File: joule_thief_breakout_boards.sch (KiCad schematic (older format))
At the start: 13 parts

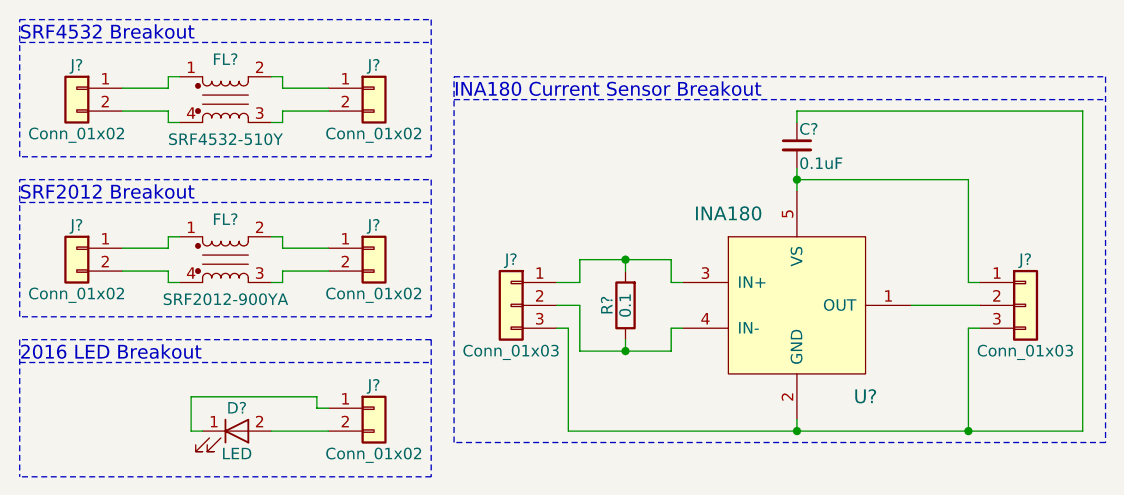
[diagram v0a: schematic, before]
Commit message: header pin swaping for easy lineup with pcb
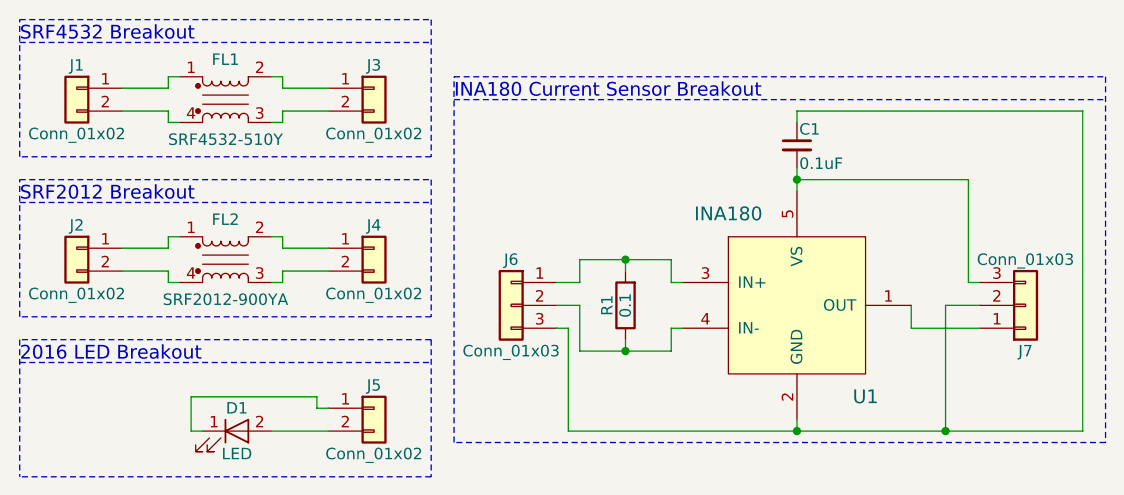
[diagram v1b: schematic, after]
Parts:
- C1: renamed from C?; footprint (none) -> Capacitors_SMD:C_0805_HandSoldering
- J1, J2, J3, J4, J5: renamed from J?; footprint (none) -> lib_fp:Etch_Pin_Header_Straight_1x02_Pitch2.54mm
- J6, J7: renamed from J?; footprint (none) -> lib_fp:Etch_Pin_Header_Straight_1x03_Pitch2.54mm
- R1: renamed from R?; footprint (none) -> Resistors_SMD:R_0805_HandSoldering
- U1: renamed from U?; footprint (none) -> TO_SOT_Packages_SMD:SOT-23-5_HandSoldering
- gave numbers to parts that had none: 3
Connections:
- net at U1.1 (OUT): now also J7.1 (Pin_1); no longer J7.2 (Pin_2)
- net at C1.1, J6.3 (Pin_3), U1.2 (GND): now also J7.2 (Pin_2); no longer J7.3 (Pin_3)
- net at C1.2, U1.5 (VS): now also J7.3 (Pin_3); no longer J7.1 (Pin_1)
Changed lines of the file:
@@
 LIBS:Bourns_EMI_Filter
 LIBS:Texas_Instruments
+LIBS:joule_thief_breakout_boards
 LIBS:power
 LIBS:device
@@
 $EndDescr
 $Comp
-L Bourns_Common_Mode_Inductor FL?
+L Bourns_Common_Mode_Inductor FL1
 U 1 1 59D17B36
 P 4200 3550
-F 0 "FL?" H 4200 3725 50  0000 C CNN
+F 0 "FL1" H 4200 3725 50  0000 C CNN
 F 1 "SRF4532-510Y" H 4200 3375 50  0000 C CNN
 F 2 "lib_fp:SRF4532_Bourns_CMI" V 4200 3590 50  0001 C CNN
@@
 $EndComp
 $Comp
-L Conn_01x02 J?
+L Conn_01x02 J3
 U 1 1 59D17D93
 P 4850 3500
-F 0 "J?" H 4850 3600 50  0000 C CNN
+F 0 "J3" H 4850 3600 50  0000 C CNN
 F 1 "Conn_01x02" H 4850 3300 50  0000 C CNN
-F 2 "" H 4850 3500 50  0001 C CNN
+F 2 "lib_fp:Etch_Pin_Header_Straight_1x02_Pitch2.54mm" H 4850 3500 50  0001 C CNN
 F 3 "" H 4850 3500 50  0001 C CNN
 	1    4850 3500
@@
 $EndComp
 $Comp
-L Conn_01x02 J?
+L Conn_01x02 J1
 U 1 1 59D17DBE
 P 3550 3500
-F 0 "J?" H 3550 3600 50  0000 C CNN
+F 0 "J1" H 3550 3600 50  0000 C CNN
 F 1 "Conn_01x02" H 3550 3300 50  0000 C CNN
-F 2 "" H 3550 3500 50  0001 C CNN
+F 2 "lib_fp:Etch_Pin_Header_Straight_1x02_Pitch2.54mm" H 3550 3500 50  0001 C CNN
 F 3 "" H 3550 3500 50  0001 C CNN
 	1    3550 3500
@@
 $EndComp
 $Comp
-L Bourns_Common_Mode_Inductor FL?
+L Bourns_Common_Mode_Inductor FL2
 U 1 1 59D17E74
 P 4200 4250
-F 0 "FL?" H 4200 4425 50  0000 C CNN
+F 0 "FL2" H 4200 4425 50  0000 C CNN
 F 1 "SRF2012-900YA" H 4200 4075 50  0000 C CNN
 F 2 "lib_fp:SRF2012_Bourns_CMI" V 4200 4290 50  0001 C CNN
@@
 $EndComp
 $Comp
-L Conn_01x02 J?
+L Conn_01x02 J4
 U 1 1 59D17E7A
 P 4850 4200
-F 0 "J?" H 4850 4300 50  0000 C CNN
+F 0 "J4" H 4850 4300 50  0000 C CNN
 F 1 "Conn_01x02" H 4850 4000 50  0000 C CNN
-F 2 "" H 4850 4200 50  0001 C CNN
+F 2 "lib_fp:Etch_Pin_Header_Straight_1x02_Pitch2.54mm" H 4850 4200 50  0001 C CNN
 F 3 "" H 4850 4200 50  0001 C CNN
 	1    4850 4200
@@
 $EndComp
 $Comp
-L Conn_01x02 J?
+L Conn_01x02 J2
 U 1 1 59D17E80
 P 3550 4200
-F 0 "J?" H 3550 4300 50  0000 C CNN
+F 0 "J2" H 3550 4300 50  0000 C CNN
 F 1 "Conn_01x02" H 3550 4000 50  0000 C CNN
-F 2 "" H 3550 4200 50  0001 C CNN
+F 2 "lib_fp:Etch_Pin_Header_Straight_1x02_Pitch2.54mm" H 3550 4200 50  0001 C CNN
 F 3 "" H 3550 4200 50  0001 C CNN
 	1    3550 4200
@@
 SRF2012 Breakout
 $Comp
-L LED D?
+L LED D1
 U 1 1 59D18B6B
 P 4250 5000
-F 0 "D?" H 4250 5100 50  0000 C CNN
+F 0 "D1" H 4250 5100 50  0000 C CNN
 F 1 "LED" H 4250 4900 50  0000 C CNN
 F 2 "lib_fp:LED_Luminus_MP-2016" H 4250 5000 50  0001 C CNN
@@
 $EndComp
 $Comp
-L Conn_01x02 J?
+L Conn_01x02 J5
 U 1 1 59D18CBF
 P 4850 4900
-F 0 "J?" H 4850 5000 50  0000 C CNN
+F 0 "J5" H 4850 5000 50  0000 C CNN
 F 1 "Conn_01x02" H 4850 4700 50  0000 C CNN
-F 2 "" H 4850 4900 50  0001 C CNN
+F 2 "lib_fp:Etch_Pin_Header_Straight_1x02_Pitch2.54mm" H 4850 4900 50  0001 C CNN
 F 3 "" H 4850 4900 50  0001 C CNN
 	1    4850 4900
@@
 2016 LED Breakout
 $Comp
-L INA180 U?
+L INA180 U1
 U 1 1 59D19901
 P 6700 4450
-F 0 "U?" H 7000 4050 60  0000 C CNN
+F 0 "U1" H 7000 4050 60  0000 C CNN
 F 1 "INA180" H 6400 4850 60  0000 C CNN
-F 2 "" H 6700 4450 60  0001 C CNN
+F 2 "TO_SOT_Packages_SMD:SOT-23-5_HandSoldering" H 6700 4450 60  0001 C CNN
 F 3 "" H 6700 4450 60  0001 C CNN
 	1    6700 4450
@@
 $EndComp
 $Comp
-L R R?
+L R R1
 U 1 1 59D19976
 P 5950 4450
-F 0 "R?" V 6030 4450 50  0000 C CNN
+F 0 "R1" V 6030 4450 50  0000 C CNN
 F 1 "0.1" V 5950 4450 50  0000 C CNN
-F 2 "" V 5880 4450 50  0001 C CNN
+F 2 "Resistors_SMD:R_0805_HandSoldering" V 5880 4450 50  0001 C CNN
 F 3 "" H 5950 4450 50  0001 C CNN
 F 4 "NONE" H 5950 4450 60  0001 C CNN "Manufacture"
@@
 $EndComp
 $Comp
-L Conn_01x03 J?
+L Conn_01x03 J7
 U 1 1 59D19C5E
 P 7700 4450
-F 0 "J?" H 7700 4650 50  0000 C CNN
+F 0 "J7" H 7700 4650 50  0000 C CNN
 F 1 "Conn_01x03" H 7700 4250 50  0000 C CNN
-F 2 "" H 7700 4450 50  0001 C CNN
+F 2 "lib_fp:Etch_Pin_Header_Straight_1x03_Pitch2.54mm" H 7700 4450 50  0001 C CNN
 F 3 "" H 7700 4450 50  0001 C CNN
 	1    7700 4450
-	1    0    0    -1
-$EndComp
-$Comp
-L Conn_01x03 J?
+	1    0    0    1
+$EndComp
+$Comp
+L Conn_01x03 J6
 U 1 1 59D19CC2
 P 5450 4450
-F 0 "J?" H 5450 4650 50  0000 C CNN
+F 0 "J6" H 5450 4650 50  0000 C CNN
 F 1 "Conn_01x03" H 5450 4250 50  0000 C CNN
-F 2 "" H 5450 4450 50  0001 C CNN
+F 2 "lib_fp:Etch_Pin_Header_Straight_1x03_Pitch2.54mm" H 5450 4450 50  0001 C CNN
 F 3 "" H 5450 4450 50  0001 C CNN
 	1    5450 4450
@@
 $EndComp
 $Comp
-L C_Small C?
+L C_Small C1
 U 1 1 59D1A6E2
 P 6700 3750
-F 0 "C?" H 6710 3820 50  0000 L CNN
+F 0 "C1" H 6710 3820 50  0000 L CNN
 F 1 "0.1uF" H 6710 3670 50  0000 L CNN
-F 2 "" H 6700 3750 50  0001 C CNN
+F 2 "Capacitors_SMD:C_0805_HandSoldering" H 6700 3750 50  0001 C CNN
 F 3 "" H 6700 3750 50  0001 C CNN
 F 4 "NONE" H 6700 3750 60  0001 C CNN "Manufacture"
@@
 Connection ~ 5950 4250
 Wire Wire Line
-	7200 4450 7500 4450
-Wire Wire Line
 	7500 4350 7450 4350
 Wire Wire Line
@@
 Wire Wire Line
 	6700 3850 6700 3950
-Wire Wire Line
-	7500 4550 7450 4550
-Wire Wire Line
-	7450 4550 7450 5000
 Wire Wire Line
 	5700 5000 7950 5000
@@
 Wire Wire Line
 	7950 3600 7950 5000
-Connection ~ 7450 5000
+Connection ~ 7350 5000
 Text Notes 5200 3550 0    60   ~ 0
 INA180 Current Sensor Breakout
@@
 Wire Notes Line
 	5200 3450 8050 3450
+Wire Wire Line
+	7350 5000 7350 4450
+Wire Wire Line
+	7350 4450 7500 4450
+Wire Wire Line
+	7200 4450 7200 4550
+Wire Wire Line
+	7200 4550 7500 4550
 $EndSCHEMATC

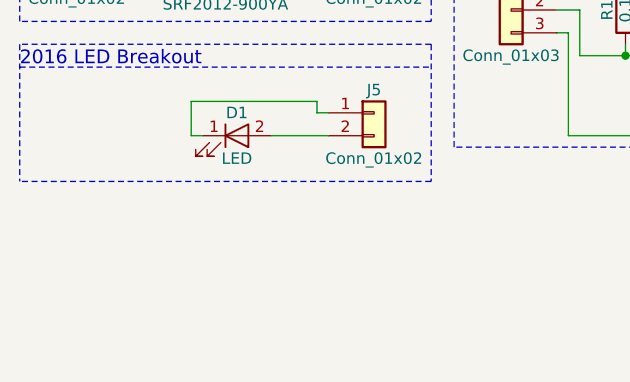
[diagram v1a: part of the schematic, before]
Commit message: add transistor breakout
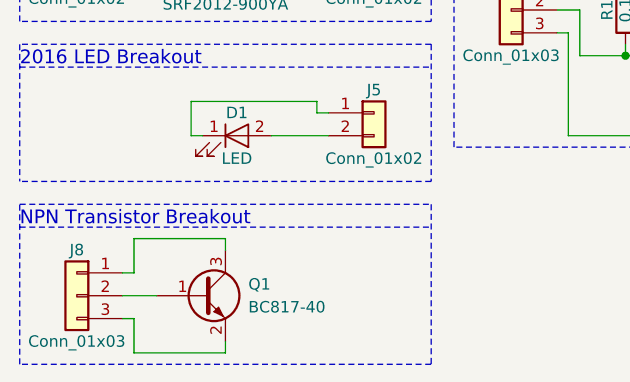
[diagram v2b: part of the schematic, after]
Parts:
- added J8: Conn_01x03, Pin_Headers:Pin_Header_Straight_1x03_Pitch2.54mm, symbol Conn_01x03
- added Q1: BC817-40, TO_SOT_Packages_SMD:SOT-23, symbol Q_NPN_BEC
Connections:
- new net: J8.2 (Pin_2), Q1.1 (B)
- new net: J8.3 (Pin_3), Q1.2 (E)
- new net: J8.1 (Pin_1), Q1.3 (C)
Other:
- note added: "NPN Transistor Breakout"
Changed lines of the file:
@@
 Wire Wire Line
 	7200 4550 7500 4550
+$Comp
+L Q_NPN_BEC Q1
+U 1 1 59D6C9FE
+P 4100 5700
+F 0 "Q1" H 4300 5750 50  0000 L CNN
+F 1 "BC817-40" H 4300 5650 50  0000 L CNN
+F 2 "TO_SOT_Packages_SMD:SOT-23" H 4300 5800 50  0001 C CNN
+F 3 "" H 4100 5700 50  0001 C CNN
+F 4 "NONE" H 4100 5700 60  0001 C CNN "Manufacture"
+F 5 "NONE" H 4100 5700 60  0001 C CNN "Mfg Part Number"
+F 6 "NONE" H 4100 5700 60  0001 C CNN "Package"
+F 7 "NONE" H 4100 5700 60  0001 C CNN "Description"
+	1    4100 5700
+	1    0    0    -1
+$EndComp
+$Comp
+L Conn_01x03 J8
+U 1 1 59D6CDE7
+P 3550 5700
+F 0 "J8" H 3550 5900 50  0000 C CNN
+F 1 "Conn_01x03" H 3550 5500 50  0000 C CNN
+F 2 "Pin_Headers:Pin_Header_Straight_1x03_Pitch2.54mm" H 3550 5700 50  0001 C CNN
+F 3 "" H 3550 5700 50  0001 C CNN
+	1    3550 5700
+	-1   0    0    -1
+$EndComp
+Wire Wire Line
+	3750 5700 3900 5700
+Wire Wire Line
+	3750 5600 3800 5600
+Wire Wire Line
+	3800 5600 3800 5450
+Wire Wire Line
+	3800 5450 4200 5450
+Wire Wire Line
+	4200 5450 4200 5500
+Wire Wire Line
+	3750 5800 3800 5800
+Wire Wire Line
+	3800 5800 3800 5950
+Wire Wire Line
+	3800 5950 4200 5950
+Wire Wire Line
+	4200 5950 4200 5900
+Text Notes 3300 5400 0    60   ~ 0
+NPN Transistor Breakout
+Wire Notes Line
+	3300 5400 5100 5400
+Wire Notes Line
+	5100 5300 5100 6000
+Wire Notes Line
+	5100 6000 3300 6000
+Wire Notes Line
+	3300 6000 3300 5300
+Wire Notes Line
+	3300 5300 5100 5300
 $EndSCHEMATC

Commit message: update CvPCB to reflect header footprint change in Pcbnew
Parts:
- J8: footprint Pin_Headers:Pin_Header_Straight_1x03_Pitch2.54mm -> lib_fp:Etch_Pin_Header_Straight_1x03_Pitch2.54mm
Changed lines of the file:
@@
 F 0 "J8" H 3550 5900 50  0000 C CNN
 F 1 "Conn_01x03" H 3550 5500 50  0000 C CNN
-F 2 "Pin_Headers:Pin_Header_Straight_1x03_Pitch2.54mm" H 3550 5700 50  0001 C CNN
+F 2 "lib_fp:Etch_Pin_Header_Straight_1x03_Pitch2.54mm" H 3550 5700 50  0001 C CNN
 F 3 "" H 3550 5700 50  0001 C CNN
 	1    3550 5700

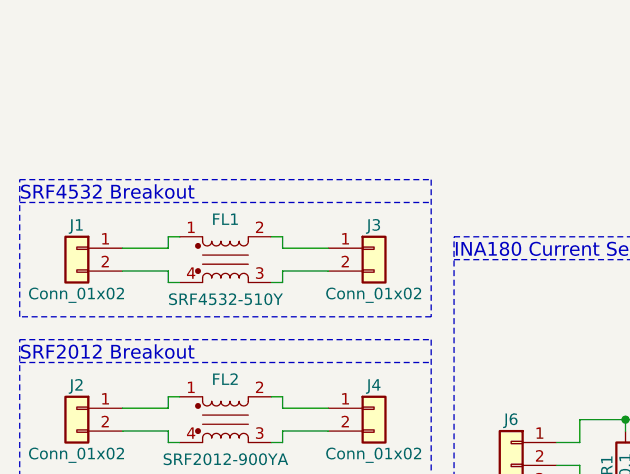
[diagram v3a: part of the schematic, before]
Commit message: add SRF3216 breakout
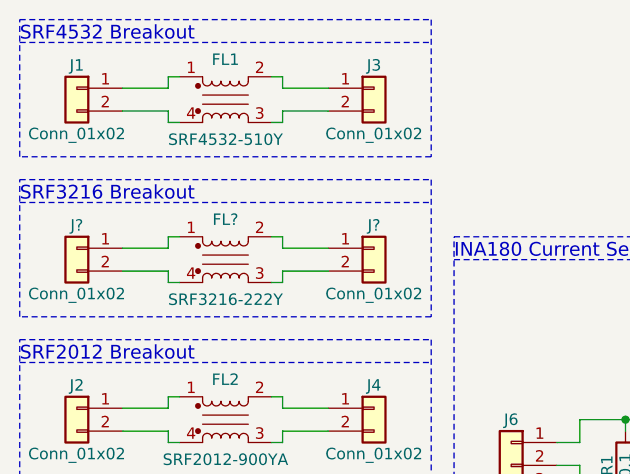
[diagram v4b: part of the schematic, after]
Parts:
- added FL?: SRF3216-222Y, lib_fp:SRF3216_Bourns_CMI, symbol Bourns_Common_Mode_Inductor
- added J? (x2): Conn_01x02, lib_fp:Etch_Pin_Header_Straight_1x02_Pitch2.54mm, symbol Conn_01x02
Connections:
- new net: FL?.1, J?.1 (Pin_1)
- new net: FL?.2, J?.1 (Pin_1)
- new net: FL?.3, J?.2 (Pin_2)
- new net: FL?.4, J?.2 (Pin_2)
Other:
- note added: "SRF3216 Breakout"
- moved on the sheet: FL1, J1, J3
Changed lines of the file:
@@
 L Bourns_Common_Mode_Inductor FL1
 U 1 1 59D17B36
-P 4200 3550
-F 0 "FL1" H 4200 3725 50  0000 C CNN
-F 1 "SRF4532-510Y" H 4200 3375 50  0000 C CNN
-F 2 "lib_fp:SRF4532_Bourns_CMI" V 4200 3590 50  0001 C CNN
-F 3 "" V 4200 3590 50  0000 C CNN
-F 4 "Bourns" H 4200 3550 60  0001 C CNN "Manufacture"
-F 5 "SRF4532-510Y" H 4200 3550 60  0001 C CNN "Mfg Part Number"
-F 6 "4532" H 4200 3550 60  0001 C CNN "Package"
-F 7 "Common Mode Chip Inductor" H 4200 3550 60  0001 C CNN "Description"
-	1    4200 3550
+P 4200 2850
+F 0 "FL1" H 4200 3025 50  0000 C CNN
+F 1 "SRF4532-510Y" H 4200 2675 50  0000 C CNN
+F 2 "lib_fp:SRF4532_Bourns_CMI" V 4200 2890 50  0001 C CNN
+F 3 "" V 4200 2890 50  0000 C CNN
+F 4 "Bourns" H 4200 2850 60  0001 C CNN "Manufacture"
+F 5 "SRF4532-510Y" H 4200 2850 60  0001 C CNN "Mfg Part Number"
+F 6 "4532" H 4200 2850 60  0001 C CNN "Package"
+F 7 "Common Mode Chip Inductor" H 4200 2850 60  0001 C CNN "Description"
+	1    4200 2850
 	1    0    0    -1
 $EndComp
@@
 L Conn_01x02 J3
 U 1 1 59D17D93
-P 4850 3500
-F 0 "J3" H 4850 3600 50  0000 C CNN
-F 1 "Conn_01x02" H 4850 3300 50  0000 C CNN
-F 2 "lib_fp:Etch_Pin_Header_Straight_1x02_Pitch2.54mm" H 4850 3500 50  0001 C CNN
-F 3 "" H 4850 3500 50  0001 C CNN
-	1    4850 3500
+P 4850 2800
+F 0 "J3" H 4850 2900 50  0000 C CNN
+F 1 "Conn_01x02" H 4850 2600 50  0000 C CNN
+F 2 "lib_fp:Etch_Pin_Header_Straight_1x02_Pitch2.54mm" H 4850 2800 50  0001 C CNN
+F 3 "" H 4850 2800 50  0001 C CNN
+	1    4850 2800
 	1    0    0    -1
 $EndComp
@@
 L Conn_01x02 J1
 U 1 1 59D17DBE
-P 3550 3500
-F 0 "J1" H 3550 3600 50  0000 C CNN
-F 1 "Conn_01x02" H 3550 3300 50  0000 C CNN
-F 2 "lib_fp:Etch_Pin_Header_Straight_1x02_Pitch2.54mm" H 3550 3500 50  0001 C CNN
-F 3 "" H 3550 3500 50  0001 C CNN
-	1    3550 3500
+P 3550 2800
+F 0 "J1" H 3550 2900 50  0000 C CNN
+F 1 "Conn_01x02" H 3550 2600 50  0000 C CNN
+F 2 "lib_fp:Etch_Pin_Header_Straight_1x02_Pitch2.54mm" H 3550 2800 50  0001 C CNN
+F 3 "" H 3550 2800 50  0001 C CNN
+	1    3550 2800
 	-1   0    0    -1
 $EndComp
@@
 	-1   0    0    -1
 $EndComp
-Text Notes 3300 3300 0    60   ~ 0
+Text Notes 3300 2600 0    60   ~ 0
 SRF4532 Breakout
 Text Notes 3300 4000 0    60   ~ 0
@@
 $EndComp
 Wire Wire Line
-	3750 3500 3950 3500
-Wire Wire Line
-	3950 3500 3950 3450
-Wire Wire Line
-	3950 3450 4000 3450
-Wire Wire Line
-	3750 3600 3950 3600
-Wire Wire Line
-	3950 3600 3950 3650
-Wire Wire Line
-	3950 3650 4000 3650
-Wire Wire Line
-	4650 3500 4450 3500
-Wire Wire Line
-	4450 3500 4450 3450
-Wire Wire Line
-	4450 3450 4400 3450
-Wire Wire Line
-	4450 3600 4650 3600
-Wire Wire Line
-	4450 3600 4450 3650
-Wire Wire Line
-	4450 3650 4400 3650
-Wire Notes Line
-	3300 3300 5100 3300
-Wire Notes Line
-	5100 3200 5100 3800
-Wire Notes Line
-	5100 3800 3300 3800
-Wire Notes Line
-	3300 3800 3300 3200
-Wire Notes Line
-	3300 3200 5100 3200
+	3750 2800 3950 2800
+Wire Wire Line
+	3950 2800 3950 2750
+Wire Wire Line
+	3950 2750 4000 2750
+Wire Wire Line
+	3750 2900 3950 2900
+Wire Wire Line
+	3950 2900 3950 2950
+Wire Wire Line
+	3950 2950 4000 2950
+Wire Wire Line
+	4650 2800 4450 2800
+Wire Wire Line
+	4450 2800 4450 2750
+Wire Wire Line
+	4450 2750 4400 2750
+Wire Wire Line
+	4450 2900 4650 2900
+Wire Wire Line
+	4450 2900 4450 2950
+Wire Wire Line
+	4450 2950 4400 2950
+Wire Notes Line
+	3300 2600 5100 2600
+Wire Notes Line
+	5100 2500 5100 3100
+Wire Notes Line
+	5100 3100 3300 3100
+Wire Notes Line
+	3300 3100 3300 2500
+Wire Notes Line
+	3300 2500 5100 2500
 Wire Wire Line
 	3750 4200 3950 4200
@@
 Wire Notes Line
 	3300 5300 5100 5300
+$Comp
+L Bourns_Common_Mode_Inductor FL?
+U 1 1 59E25E9F
+P 4200 3550
+F 0 "FL?" H 4200 3725 50  0000 C CNN
+F 1 "SRF3216-222Y" H 4200 3375 50  0000 C CNN
+F 2 "lib_fp:SRF3216_Bourns_CMI" V 4200 3590 50  0001 C CNN
+F 3 "" V 4200 3590 50  0000 C CNN
+F 4 "Bourns" H 4200 3550 60  0001 C CNN "Manufacture"
+F 5 "SRF3216-222Y" H 4200 3550 60  0001 C CNN "Mfg Part Number"
+F 6 "3216" H 4200 3550 60  0001 C CNN "Package"
+F 7 "Common Mode Chip Inductor" H 4200 3550 60  0001 C CNN "Description"
+	1    4200 3550
+	1    0    0    -1
+$EndComp
+$Comp
+L Conn_01x02 J?
+U 1 1 59E25EA5
+P 4850 3500
+F 0 "J?" H 4850 3600 50  0000 C CNN
+F 1 "Conn_01x02" H 4850 3300 50  0000 C CNN
+F 2 "lib_fp:Etch_Pin_Header_Straight_1x02_Pitch2.54mm" H 4850 3500 50  0001 C CNN
+F 3 "" H 4850 3500 50  0001 C CNN
+	1    4850 3500
+	1    0    0    -1
+$EndComp
+$Comp
+L Conn_01x02 J?
+U 1 1 59E25EAB
+P 3550 3500
+F 0 "J?" H 3550 3600 50  0000 C CNN
+F 1 "Conn_01x02" H 3550 3300 50  0000 C CNN
+F 2 "lib_fp:Etch_Pin_Header_Straight_1x02_Pitch2.54mm" H 3550 3500 50  0001 C CNN
+F 3 "" H 3550 3500 50  0001 C CNN
+	1    3550 3500
+	-1   0    0    -1
+$EndComp
+Text Notes 3300 3300 0    60   ~ 0
+SRF3216 Breakout
+Wire Wire Line
+	3750 3500 3950 3500
+Wire Wire Line
+	3950 3500 3950 3450
+Wire Wire Line
+	3950 3450 4000 3450
+Wire Wire Line
+	3750 3600 3950 3600
+Wire Wire Line
+	3950 3600 3950 3650
+Wire Wire Line
+	3950 3650 4000 3650
+Wire Wire Line
+	4650 3500 4450 3500
+Wire Wire Line
+	4450 3500 4450 3450
+Wire Wire Line
+	4450 3450 4400 3450
+Wire Wire Line
+	4450 3600 4650 3600
+Wire Wire Line
+	4450 3600 4450 3650
+Wire Wire Line
+	4450 3650 4400 3650
+Wire Notes Line
+	3300 3300 5100 3300
+Wire Notes Line
+	5100 3200 5100 3800
+Wire Notes Line
+	5100 3800 3300 3800
+Wire Notes Line
+	3300 3800 3300 3200
+Wire Notes Line
+	3300 3200 5100 3200
 $EndSCHEMATC

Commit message: annotate new componets, update net list
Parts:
- gave numbers to parts that had none: 3
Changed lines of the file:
@@
 	3300 5300 5100 5300
 $Comp
-L Bourns_Common_Mode_Inductor FL?
+L Bourns_Common_Mode_Inductor FL3
 U 1 1 59E25E9F
 P 4200 3550
-F 0 "FL?" H 4200 3725 50  0000 C CNN
+F 0 "FL3" H 4200 3725 50  0000 C CNN
 F 1 "SRF3216-222Y" H 4200 3375 50  0000 C CNN
 F 2 "lib_fp:SRF3216_Bourns_CMI" V 4200 3590 50  0001 C CNN
@@
 $EndComp
 $Comp
-L Conn_01x02 J?
+L Conn_01x02 J10
 U 1 1 59E25EA5
 P 4850 3500
-F 0 "J?" H 4850 3600 50  0000 C CNN
+F 0 "J10" H 4850 3600 50  0000 C CNN
 F 1 "Conn_01x02" H 4850 3300 50  0000 C CNN
 F 2 "lib_fp:Etch_Pin_Header_Straight_1x02_Pitch2.54mm" H 4850 3500 50  0001 C CNN
@@
 $EndComp
 $Comp
-L Conn_01x02 J?
+L Conn_01x02 J9
 U 1 1 59E25EAB
 P 3550 3500
-F 0 "J?" H 3550 3600 50  0000 C CNN
+F 0 "J9" H 3550 3600 50  0000 C CNN
 F 1 "Conn_01x02" H 3550 3300 50  0000 C CNN
 F 2 "lib_fp:Etch_Pin_Header_Straight_1x02_Pitch2.54mm" H 3550 3500 50  0001 C CNN
